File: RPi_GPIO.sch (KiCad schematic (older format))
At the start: 42 parts, among them J2 RPi_GPIO, J3 Conn_02x03_Counter_Clockwise, J5 Conn_01x03_Male, J6 Conn_01x03_Male, J7 Conn_01x03_Male, J8 Conn_01x03_Male, J9 Conn_01x03_Male, SW1 SW_Push, U2 STM32F030CCTx, U3 MAX485E, U4 MAX485E, U5 MAX485E, U6 MAX485E, U7 MAX485E

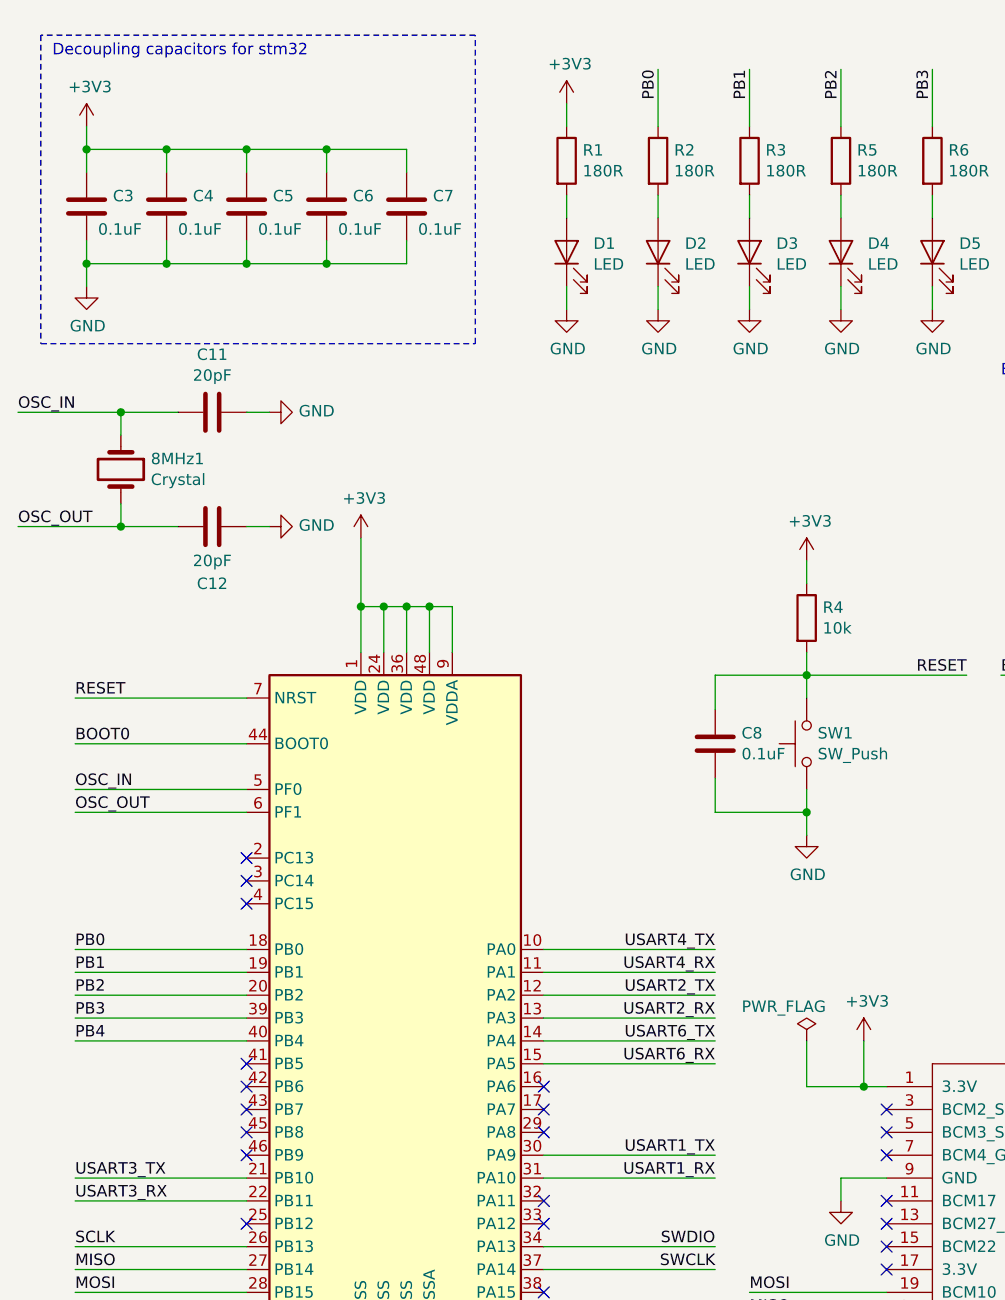
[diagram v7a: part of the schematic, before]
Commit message: Keepon routing
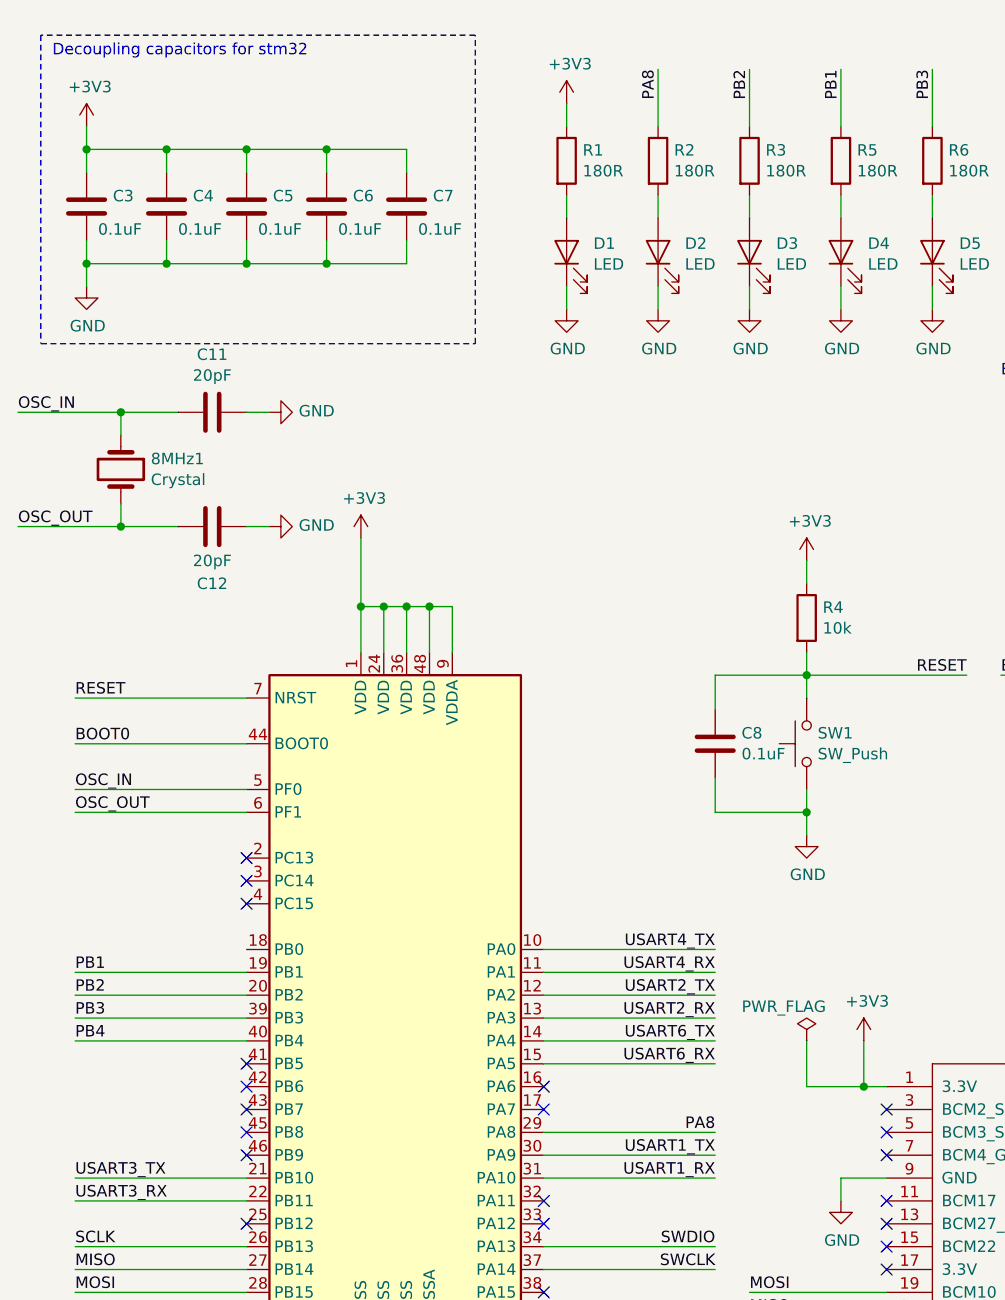
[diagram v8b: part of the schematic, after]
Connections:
- net PB1: now also R5.1; no longer R3.1
- net PB2: now also R3.1; no longer R5.1
- net PA8: now reaches U2.29 (PA8)
- net PA8: now also R2.1
- net PB0: no longer names the net of U2.18 (PB0)
- net PB0: no longer R2.1
- no-connect marks 51 -> 50
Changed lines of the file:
@@
 SCLK
 Wire Wire Line
-	1700 4700 950  4700
-Wire Wire Line
 	1700 4800 950  4800
 Wire Wire Line
@@
 Wire Wire Line
 	1700 5000 950  5000
-Text Label 950  4700 0    50   ~ 0
-PB0
 Text Label 950  4800 0    50   ~ 0
 PB1
@@
 $EndComp
 Text Label 3500 850  3    50   ~ 0
-PB0
+PA8
 $Comp
 L Device:R R3
@@
 $EndComp
 Text Label 3900 850  3    50   ~ 0
-PB1
+PB2
 $Comp
 L Device:R R5
@@
 $EndComp
 Text Label 4300 850  3    50   ~ 0
-PB2
+PB1
 $Comp
 L Device:R R6
@@
 NoConn ~ 3000 5900
 NoConn ~ 3000 5800
-NoConn ~ 3000 5500
 NoConn ~ 3000 5400
 NoConn ~ 3000 5300
@@
 	1    0    0    -1
 $EndComp
+Wire Wire Line
+	3000 5500 3750 5500
+Text Label 3750 5500 2    50   ~ 0
+PA8
 $EndSCHEMATC
